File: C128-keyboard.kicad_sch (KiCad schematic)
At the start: 116 parts, among them CN1 C128, CN2 Neo128, SW1 Inst/Del, SW10 Esc, SW11 Alt, SW12 Return, SW13 W, SW14 R, SW15 Y, SW16 I, SW17 P, SW18 *, SW19 LeftArrow, SW2 3, SW20 Num8, SW21 Num+, SW22 Num0, SW23 Crsr Horiz, SW24 A, SW25 D, SW26 G, SW27 J, SW28 L, SW29 ;, SW3 5, SW30 Ctrl, SW31 Num5, SW32 Num-, SW33 Num., SW34 F7, SW35 4, SW36 6, SW37 8, SW38 0, SW39 -, SW4 7, SW40 Clr/Home, SW41 2, SW42 Tab, SW43 LineFeed, SW44 Crsr-Up, SW45 F1, SW46 Z, SW47 C, SW48 B, SW49 M, SW5 9, SW50 ., SW51 R-Shift, SW52 Space, SW53 Num2, SW54 NumEnter, SW55 Crsr-Down, SW56 F3, SW57 S, SW58 F, SW59 H, SW6 +, SW60 K, SW61 :, SW62 =, SW63 C=, SW64 Num4, SW65 Num6, SW66 Crsr-Left, SW67 F5, SW68 E, SW69 T, SW7 £, SW70 U, SW71 O, SW72 @, SW73 UpArrow, SW74 Q, SW75 Num7, SW76 Num9, SW77 Crsr-Right, SW78 Crsr Vert, SW79 L-Shift, SW8 1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

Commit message: 7-9U combined space bar
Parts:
- SW52: footprint MX_Alps_Hybrid:MX-9U-ReversedStabilizers-NoLED -> lib_fp:MX-7_9U-ReversedStabilizers-NoLED
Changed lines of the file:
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@@
     (property "Reference" "SW52" (id 0) (at 324.485 85.09 0))
     (property "Value" "Space" (id 1) (at 324.485 87.63 0))
-    (property "Footprint" "MX_Alps_Hybrid:MX-9U-ReversedStabilizers-NoLED" (id 2) (at 324.485 93.345 0)
+    (property "Footprint" "lib_fp:MX-7_9U-ReversedStabilizers-NoLED" (id 2) (at 324.485 93.345 0)
       (effects (font (size 1.27 1.27)) hide)
     )
@@
     )
     (path "/8f2228b6-afd3-4817-adf7-5d66443588ee"
-      (reference "SW52") (unit 1) (value "Space") (footprint "MX_Alps_Hybrid:MX-9U-ReversedStabilizers-NoLED")
+      (reference "SW52") (unit 1) (value "Space") (footprint "lib_fp:MX-7_9U-ReversedStabilizers-NoLED")
     )
     (path "/788d6c18-cfab-4cf0-9b9c-9b5e11f782b2"

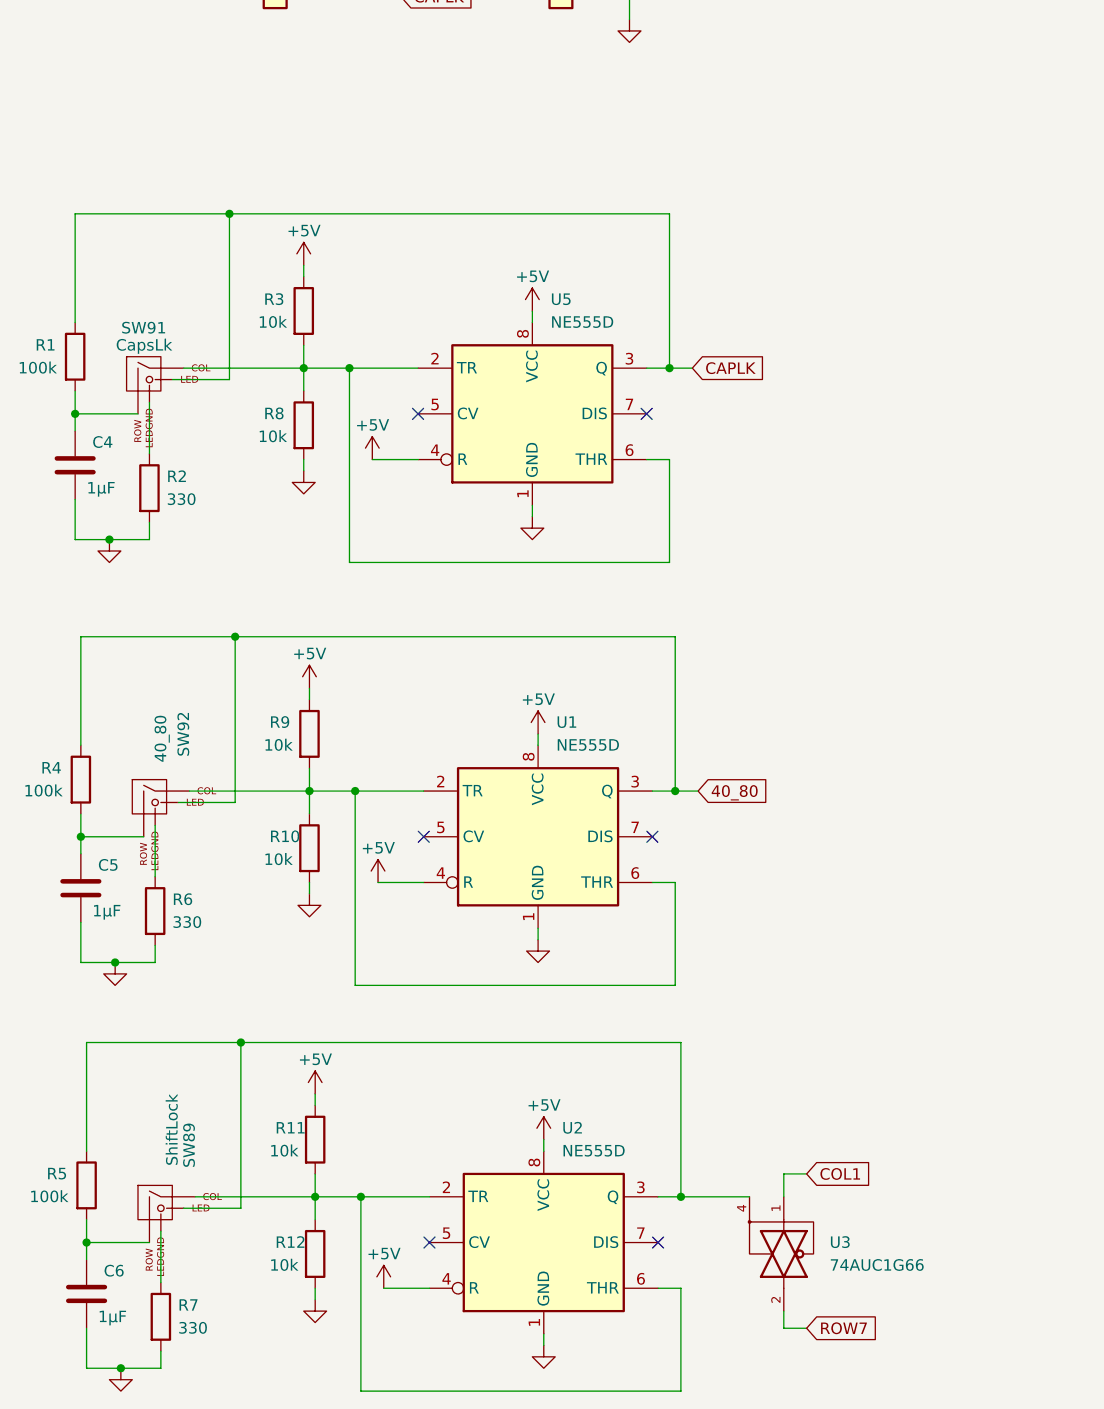
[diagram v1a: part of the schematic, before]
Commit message: Use MAX16054
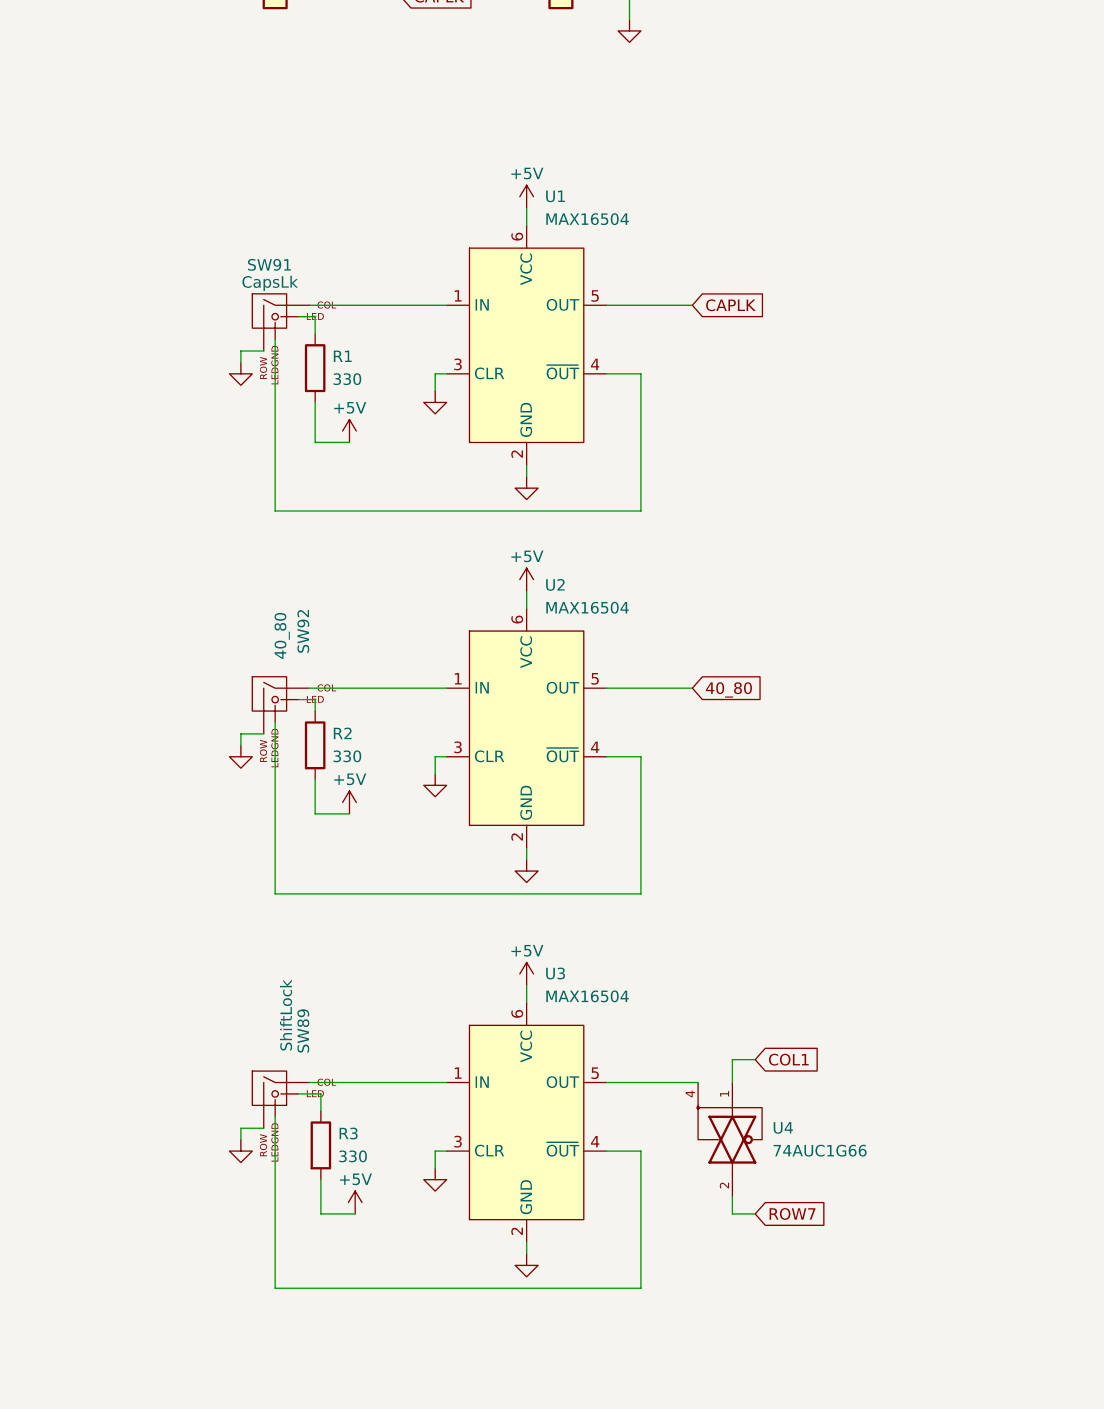
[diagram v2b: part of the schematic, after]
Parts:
- removed C4, C5, C6: 1µF, Capacitor_SMD:C_0603_1608Metric_Pad1.08x0.95mm_HandSolder, symbol Device:C
- removed R1, R4, R5: 100k, Resistor_SMD:R_0603_1608Metric_Pad0.98x0.95mm_HandSolder, symbol Device:R
- removed R10, R11, R12, R3, R8, R9: 10k, Resistor_SMD:R_0603_1608Metric_Pad0.98x0.95mm_HandSolder, symbol Device:R
- removed U1, U2, U5: NE555D, Package_SO:SOIC-8_3.9x4.9mm_P1.27mm, symbol Timer:NE555D
- added U1, U2, U3: MAX16504, Package_TO_SOT_SMD:TSOT-23-6, symbol c128keyboard:MAX16504
- C1, C2, C3: LCSC (none) -> C126556
- CN1: now left out of the parts list
- R1: renamed from R2; LCSC (none) -> C278617
- R2: renamed from R6; LCSC (none) -> C278617
- R3: renamed from R7; LCSC (none) -> C278617
- U4: renamed from U3; LCSC (none) -> C327492
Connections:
- net 40_80: now also U2.5 (OUT); no longer SW92.3 (LED)
- net CAPLK: now also U1.5 (OUT); no longer SW91.3 (LED)
- net GND: now also SW89.2 (ROW), SW91.2 (ROW), SW92.2 (ROW), U1.2 (GND), U1.3 (CLR), U2.2 (GND), U2.3 (CLR), U3.2 (GND), U3.3 (CLR); no longer R1.2, R2.2, R3.2
- net VCC: now also R1.2, R2.2, R3.2, U1.6 (VCC), U2.6 (VCC), U3.6 (VCC)
- net at SW89.1 (COL): now also U3.1 (IN)
- net at U4.4: now also U3.5 (OUT); no longer SW89.3 (LED)
- net at SW89.4 (LEDGND): now also U3.4 (~{OUT}); no longer R3.1
- net at SW92.1 (COL): now also U2.1 (IN)
- net at SW92.4 (LEDGND): now also U2.4 (~{OUT}); no longer R2.1
- net at SW91.1 (COL): now also U1.1 (IN)
- net at R1.1: now also SW91.3 (LED); no longer SW91.4 (LEDGND)
- new net: R3.1, SW89.3 (LED)
- new net: R2.1, SW92.3 (LED)
- new net: SW91.4 (LEDGND), U1.4 (~{OUT})
- no-connect marks 7 -> 1
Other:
- moved on the sheet: R1, R2, R3, SW89, SW91, SW92, U4

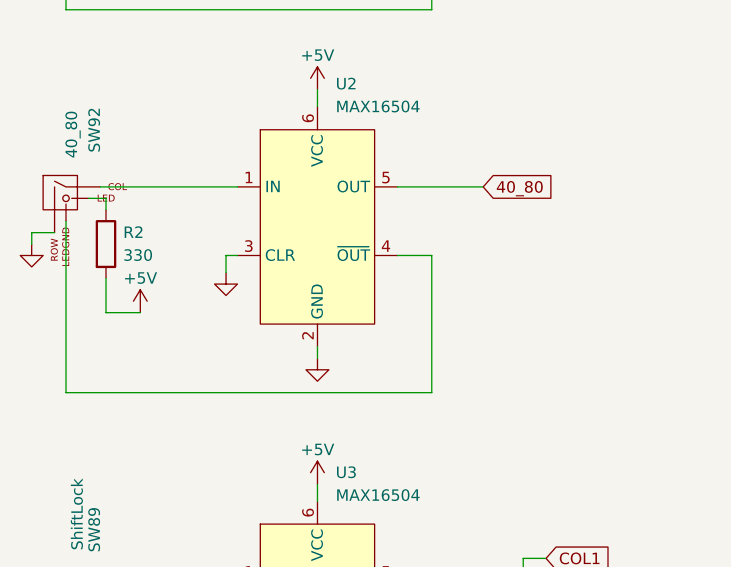
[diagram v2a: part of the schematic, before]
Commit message: Fix polarity of 40/80 key
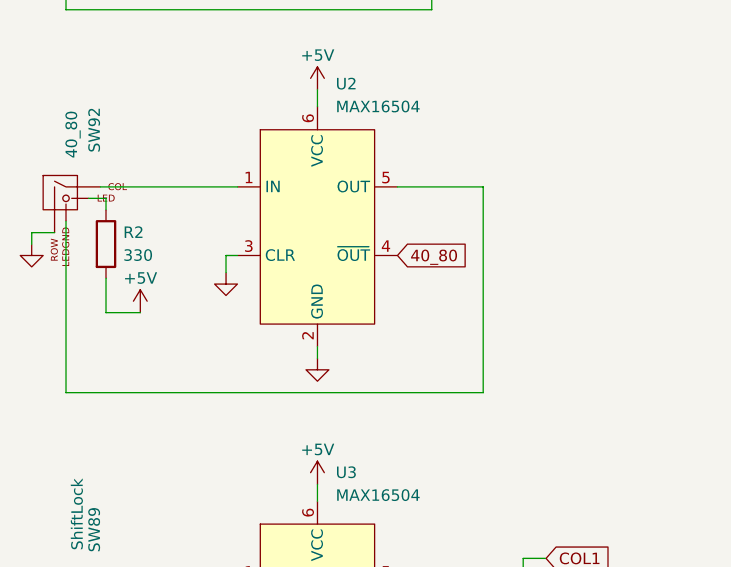
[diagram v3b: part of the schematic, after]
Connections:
- net 40_80: now also U2.4 (~{OUT}); no longer U2.5 (OUT)
- net at SW92.4 (LEDGND): now also U2.5 (OUT); no longer U2.4 (~{OUT})
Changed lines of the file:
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@@
     (stroke (width 0) (type solid) (color 0 0 0 0))
+  )
+  (wire (pts (xy 95.25 224.79) (xy 95.25 201.93))
+    (stroke (width 0) (type default) (color 0 0 0 0))
   )
   (wire (pts (xy 89.535 167.005) (xy 89.535 182.245))
@@
     (stroke (width 0) (type solid) (color 0 0 0 0))
   )
+  (wire (pts (xy 48.895 224.79) (xy 95.25 224.79))
+    (stroke (width 0) (type default) (color 0 0 0 0))
+  )
   (wire (pts (xy 53.975 97.155) (xy 62.865 97.155))
     (stroke (width 0) (type solid) (color 0 0 0 0))
@@
     (stroke (width 0) (type solid) (color 0 0 0 0))
   )
-  (wire (pts (xy 89.535 209.55) (xy 89.535 224.79))
-    (stroke (width 0) (type default) (color 0 0 0 0))
-  )
   (wire (pts (xy 85.725 117.475) (xy 92.71 117.475))
     (stroke (width 0) (type solid) (color 0 0 0 0))
   )
-  (wire (pts (xy 85.725 209.55) (xy 89.535 209.55))
-    (stroke (width 0) (type default) (color 0 0 0 0))
-  )
   (wire (pts (xy 85.725 79.375) (xy 92.71 79.375))
     (stroke (width 0) (type solid) (color 0 0 0 0))
@@
   )
   (wire (pts (xy 85.725 201.93) (xy 95.25 201.93))
-    (stroke (width 0) (type default) (color 0 0 0 0))
-  )
-  (wire (pts (xy 48.895 224.79) (xy 89.535 224.79))
     (stroke (width 0) (type default) (color 0 0 0 0))
   )
@@
     )
   )
-  (global_label "40_80" (shape input) (at 95.25 201.93 0) (fields_autoplaced)
+  (global_label "40_80" (shape input) (at 85.725 209.55 0) (fields_autoplaced)
     (effects (font (size 1.27 1.27)) (justify left))
-    (property "Intersheet References" "${INTERSHEET_REFS}" (id 0) (at 103.4688 202.0094 0)
+    (property "Intersheet References" "${INTERSHEET_REFS}" (id 0) (at 93.9438 209.6294 0)
       (effects (font (size 1.27 1.27)) (justify left) hide)
     )

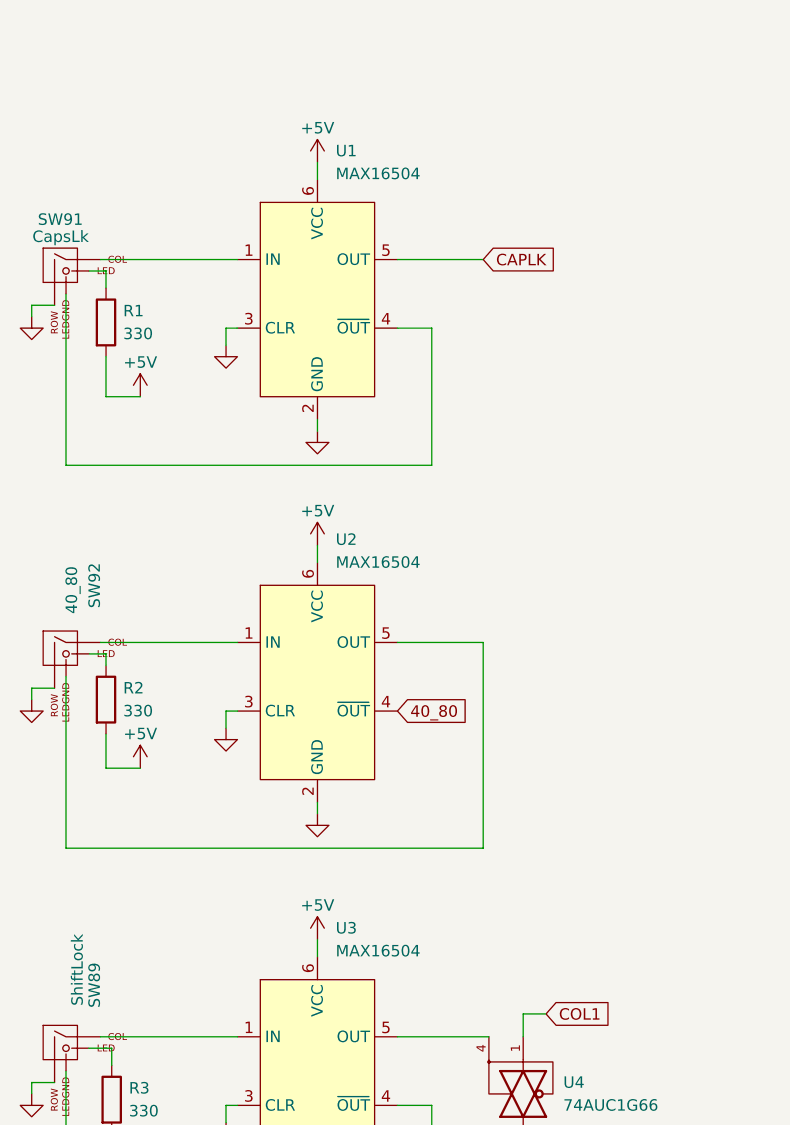
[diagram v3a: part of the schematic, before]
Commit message: Fix MAX16054 part number
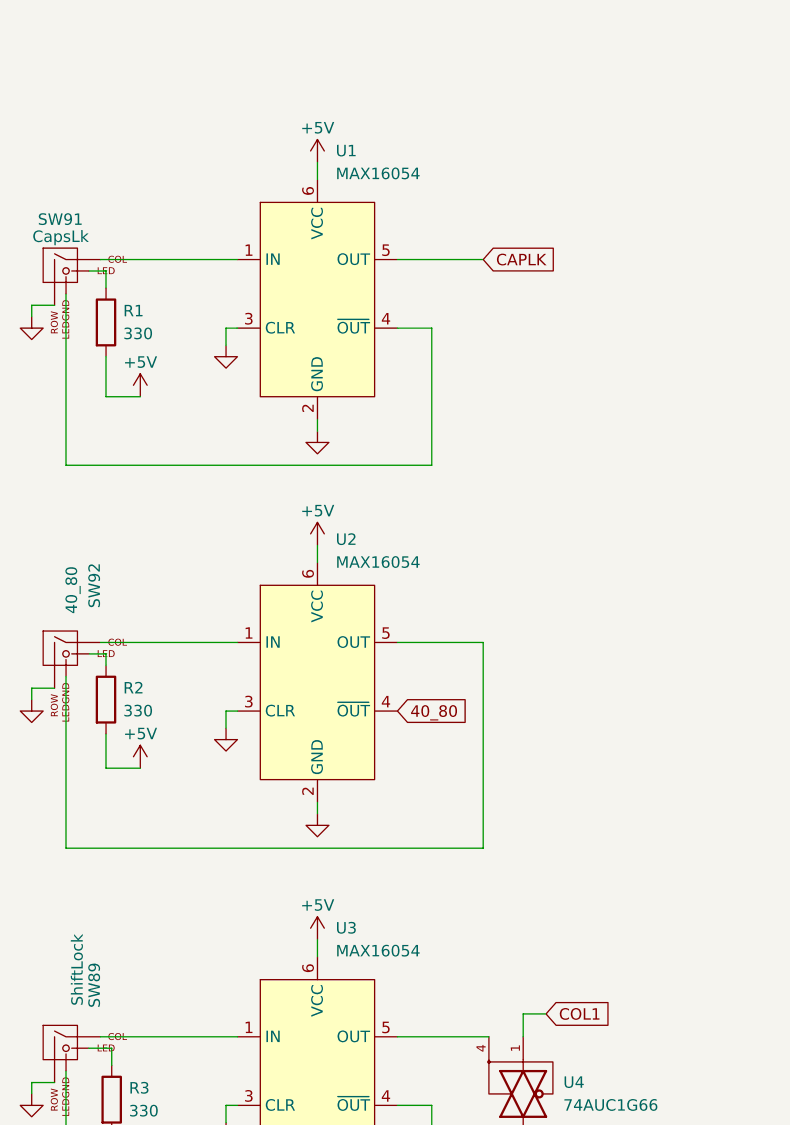
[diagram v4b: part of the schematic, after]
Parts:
- U1, U2, U3: value MAX16504 -> MAX16054; symbol c128keyboard:MAX16504 -> c128keyboard:MAX16054
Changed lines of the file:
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@@
     (pin "2")
   )
-  (symbol (lib_id "c128keyboard:MAX16504") (at 76.835 249.555 0) (unit 1)
+  (symbol (lib_id "c128keyboard:MAX16054") (at 76.835 249.555 0) (unit 1)
     (in_bom yes) (on_board yes) (fields_autoplaced)
     (property "Reference" "U3" (id 0) (at 78.8544 233.68 0)
       (effects (font (size 1.27 1.27)) (justify left))
     )
-    (property "Value" "MAX16504" (id 1) (at 78.8544 236.22 0)
+    (property "Value" "MAX16054" (id 1) (at 78.8544 236.22 0)
       (effects (font (size 1.27 1.27)) (justify left))
     )
@@
     (pin "2")
   )
-  (symbol (lib_id "c128keyboard:MAX16504") (at 76.835 205.74 0) (unit 1)
+  (symbol (lib_id "c128keyboard:MAX16054") (at 76.835 205.74 0) (unit 1)
     (in_bom yes) (on_board yes) (fields_autoplaced)
     (property "Reference" "U2" (id 0) (at 78.8544 190.5 0)
       (effects (font (size 1.27 1.27)) (justify left))
     )
-    (property "Value" "MAX16504" (id 1) (at 78.8544 193.04 0)
+    (property "Value" "MAX16054" (id 1) (at 78.8544 193.04 0)
       (effects (font (size 1.27 1.27)) (justify left))
     )
@@
     (pin "2")
   )
-  (symbol (lib_id "c128keyboard:MAX16504") (at 76.835 163.195 0) (unit 1)
+  (symbol (lib_id "c128keyboard:MAX16054") (at 76.835 163.195 0) (unit 1)
     (in_bom yes) (on_board yes) (fields_autoplaced)
     (property "Reference" "U1" (id 0) (at 78.8544 147.32 0)
       (effects (font (size 1.27 1.27)) (justify left))
     )
-    (property "Value" "MAX16504" (id 1) (at 78.8544 149.86 0)
+    (property "Value" "MAX16054" (id 1) (at 78.8544 149.86 0)
       (effects (font (size 1.27 1.27)) (justify left))
     )
@@
     )
     (path "/bbf45529-58ab-4e60-8546-7ddee3b7f812"
-      (reference "U1") (unit 1) (value "MAX16504") (footprint "Package_TO_SOT_SMD:TSOT-23-6")
+      (reference "U1") (unit 1) (value "MAX16054") (footprint "Package_TO_SOT_SMD:TSOT-23-6")
     )
     (path "/4b68979d-1715-42c2-a944-c292821126a1"
-      (reference "U2") (unit 1) (value "MAX16504") (footprint "Package_TO_SOT_SMD:TSOT-23-6")
+      (reference "U2") (unit 1) (value "MAX16054") (footprint "Package_TO_SOT_SMD:TSOT-23-6")
     )
     (path "/01e85fcc-4f6d-4841-b395-07b20af43922"
-      (reference "U3") (unit 1) (value "MAX16504") (footprint "Package_TO_SOT_SMD:TSOT-23-6")
+      (reference "U3") (unit 1) (value "MAX16054") (footprint "Package_TO_SOT_SMD:TSOT-23-6")
     )
     (path "/ffcb565f-a4bf-496d-be76-dba9790fa6ca"
